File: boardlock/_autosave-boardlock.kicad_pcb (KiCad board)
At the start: 2 copper layers, 101 x 76.2 mm, 169 parts, among them J1 Conn_01x02, J2 Conn_01x02, J3 Conn_01x02, J4 Conn_01x02, J5 5033981892, J6 USB_C_Receptacle_USB2.0, Q1 BSS84PWH6327XTSA1, Q2 MMBT4401, Q3 BSS84PWH6327XTSA1, Q4 DTC124X, Q5 DTC124X, Q6 DTC124X, Q7 DTC124X, SW1 SW_Push, SW2 SW_Push, SW3 SW_Push, SW4 SW_Push, SW5 SW_Push, U1 ESP32-S3-WROOM-1, U2 LSM6DSO32, U3 SAM-M8Q, U4 BQ24075RGT, U5 BQ27441DRZR-G1A, U6 TPS630701RNMR, U7 MCP1661, U8 MAX98357AETE+T, U9 TPD2E2U06

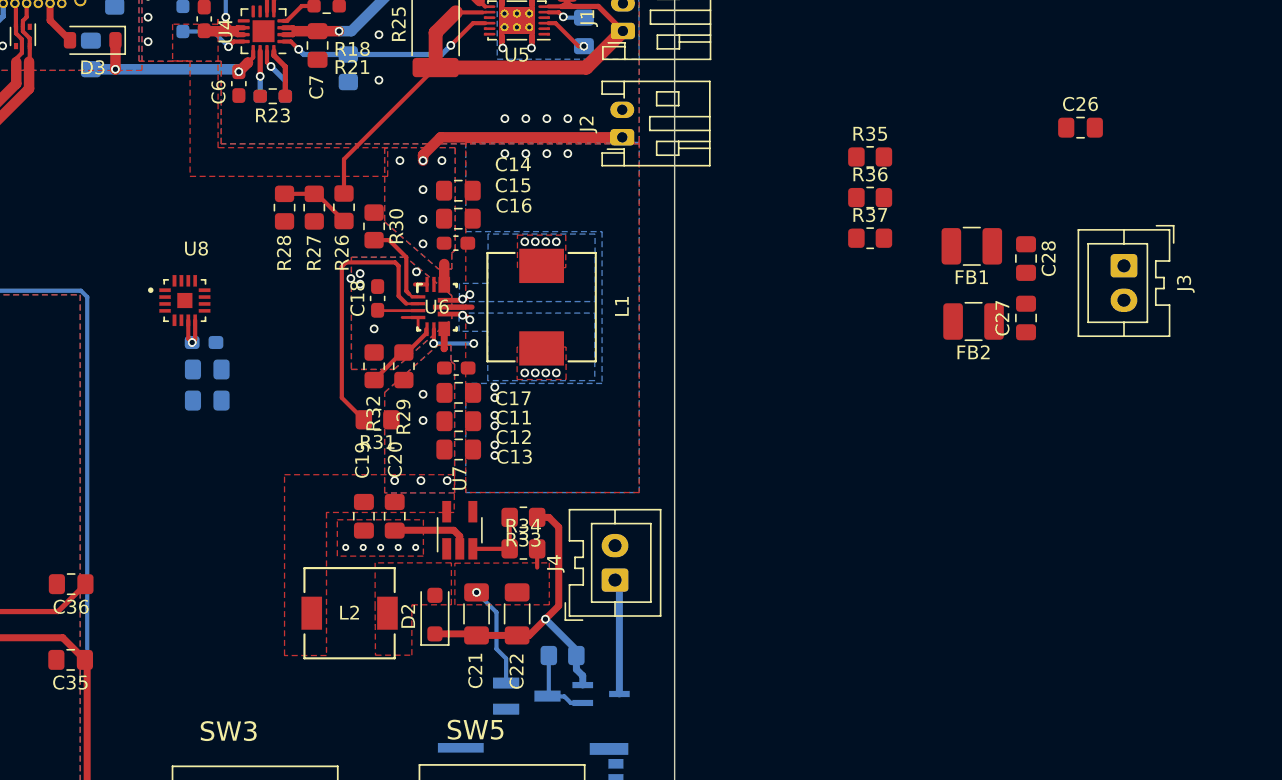
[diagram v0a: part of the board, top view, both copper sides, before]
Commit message: added LED to lock location
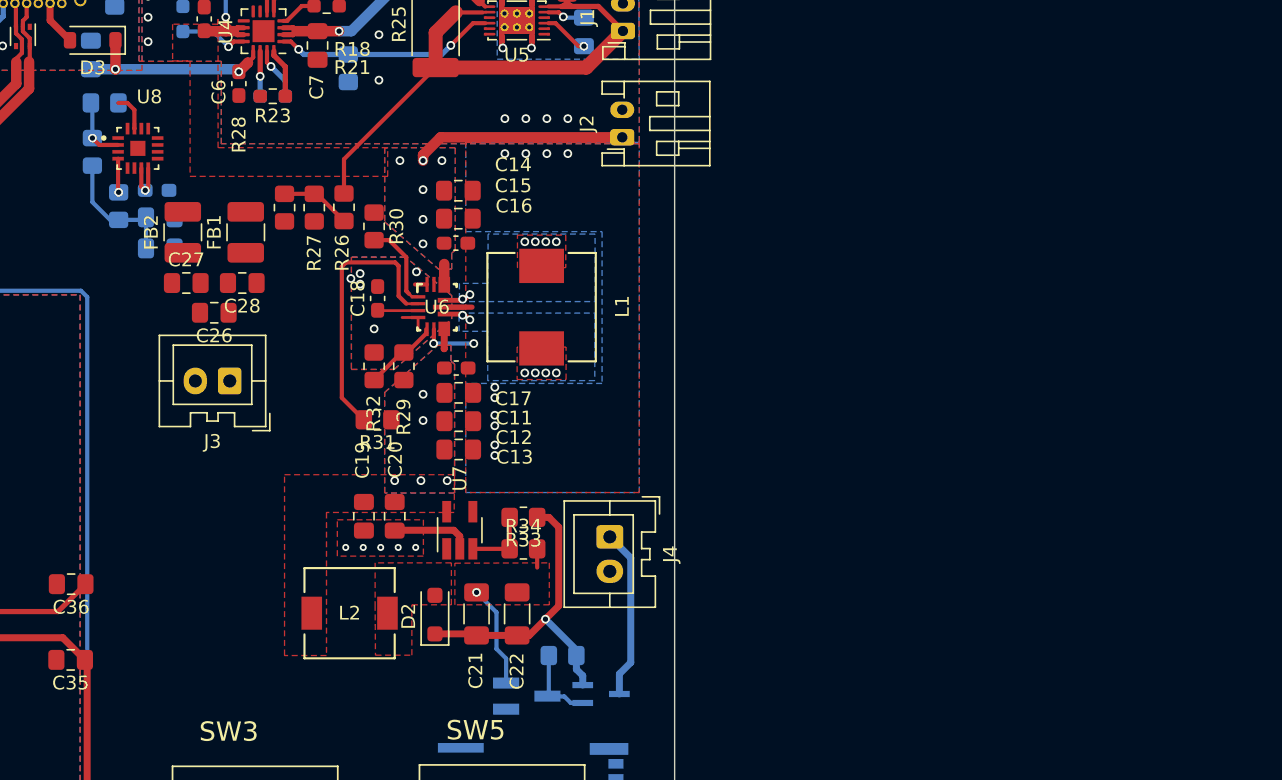
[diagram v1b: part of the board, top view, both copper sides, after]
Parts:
- R35, R36, R37: moved to B.Cu
- moved J3 65.5 mm to (175.9, 98.0), turned to 180 degrees
- moved C26 64.3 mm to (174.7, 93.1), turned to 180 degrees
- moved C27 61.0 mm to (172.7, 90.9), turned to 0 degrees
- moved FB2 57.8 mm to (172.4, 87.2), turned to 90 degrees
- moved C28 56.9 mm to (176.8, 90.9), turned to 180 degrees
- moved R35 56.5 mm to (165.9, 81.4), turned to 90 degrees
- moved R36 56.0 mm to (166.8, 77.9)
- moved R37 54.6 mm to (167.8, 85.3), turned to 90 degrees
- moved FB1 52.7 mm to (177.0, 87.2), turned to 90 degrees
- moved C25 11.6 mm to (170.6, 84.2)
- moved C24 11.6 mm to (170.8, 86.2)
- moved C23 11.6 mm to (170.8, 88.4)
- moved U8 11.6 mm to (169.2, 81.2)
- moved J4 3.16 mm to (203.5, 109.4), turned to -90 degrees
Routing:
- net +3V3: track 33.8 -> 43.2 mm
- net GAIN_SLOT: track 0.00 -> 4.67 mm, vias 0 -> 1
- net /audio/BUZZER_POWER: track 8.41 -> 12.4 mm
- net GND: track 49.2 -> 52.0 mm
- net M_AUDIO_SD_MODE: track 0.00 -> 2.46 mm, vias 0 -> 1
